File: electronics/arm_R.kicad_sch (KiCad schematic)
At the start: 26 parts, among them J10 EV3 R 4434 HOLD, J20 R SERVO G + S, U10 DRV8871DDAR, U20 SN74LVC2G17DBVR, U30 SN74AHCT1G125DBVR

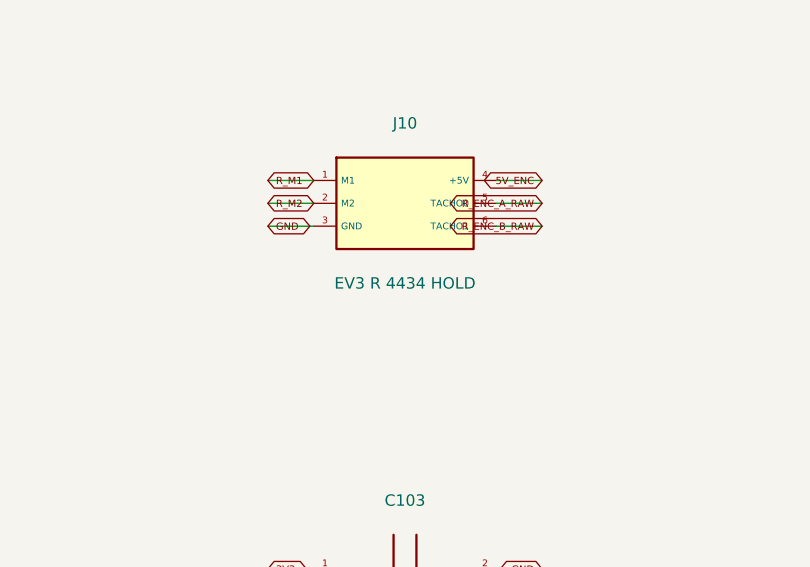
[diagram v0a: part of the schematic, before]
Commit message: Integrate onboard RP2040 and drawing-based EV3 jacks on A1 PCB
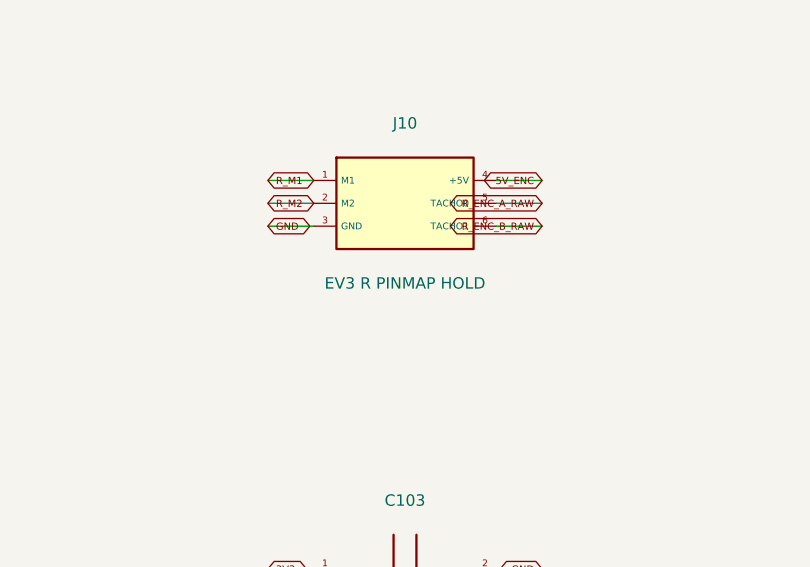
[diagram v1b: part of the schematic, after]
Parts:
- J10: value EV3 R 4434 HOLD -> EV3 R PINMAP HOLD; footprint Quadcuber:EV3_4434_PROVISIONAL -> Quadcuber:EV3_UserDrawing_PINMAP_HOLD; MPN 4434 -> UNCONFIRMED user drawing; Manufacturer Adafruit (supplier brand) -> Unconfirmed (Coorle watermark)
- TP10, TP11, TP12, TP13: now left out of the parts list
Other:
- title: Quadcuber A0 / arm_R / ENGINEERING HOLD -> Quadcuber A1 / arm_R / ENGINEERING HOLD

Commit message: Correct audited power BOM and add bounded VM discharge protection
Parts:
- C101: MPN GRM32ER71E106KA12L -> GRM32DR71E106KA12L
- F10: footprint Quadcuber:Fuse_1812_4532Metric -> Quadcuber:Fuse_Bourns_MF_MSMF_Style2_1812; MPN MF-MSMF110-2 -> MF-MSMF110/16X-2

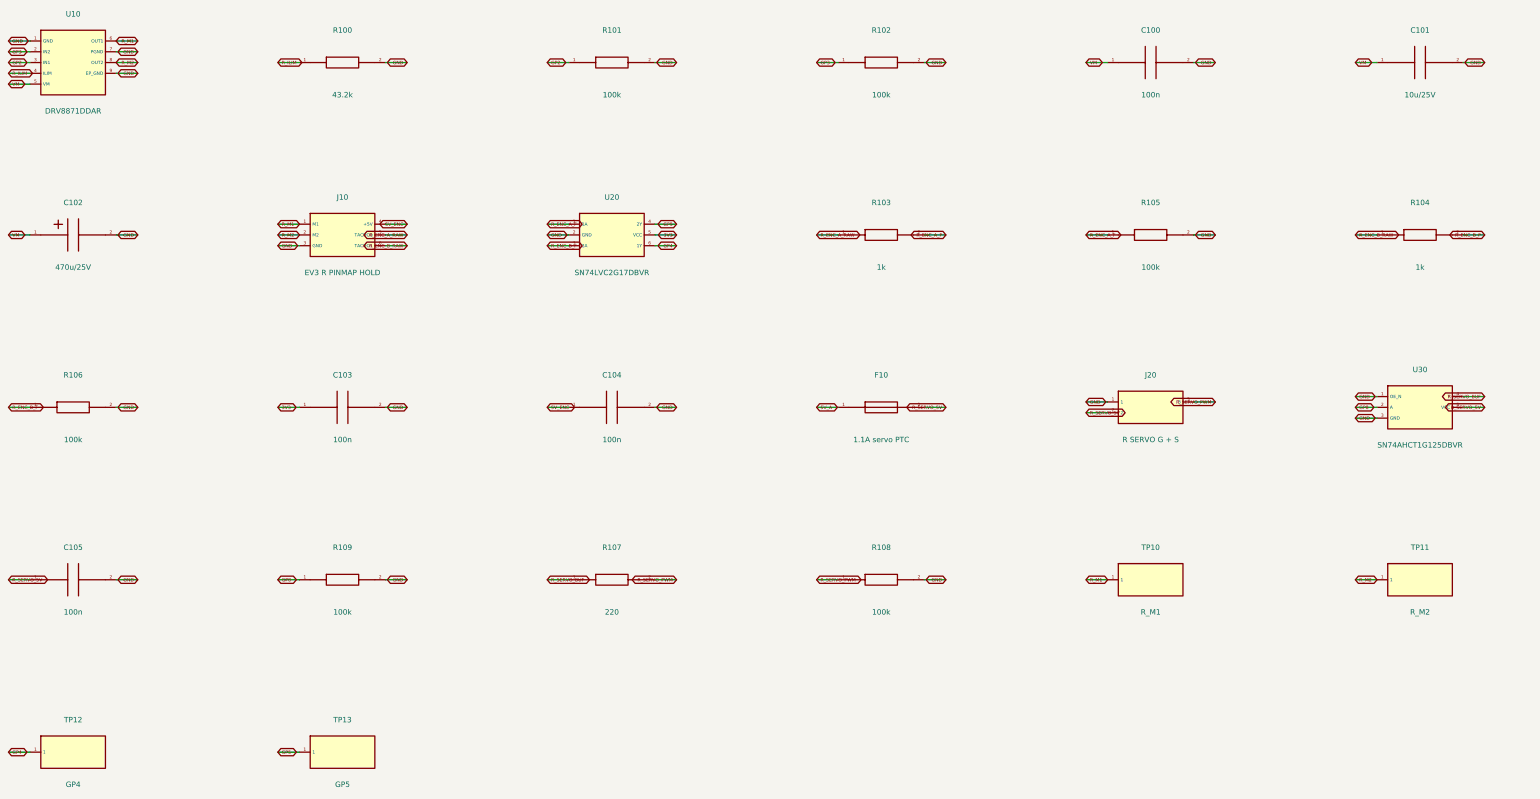
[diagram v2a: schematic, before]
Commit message: Migrate A1 to KiCad 10 and record blocked vendor-model transients
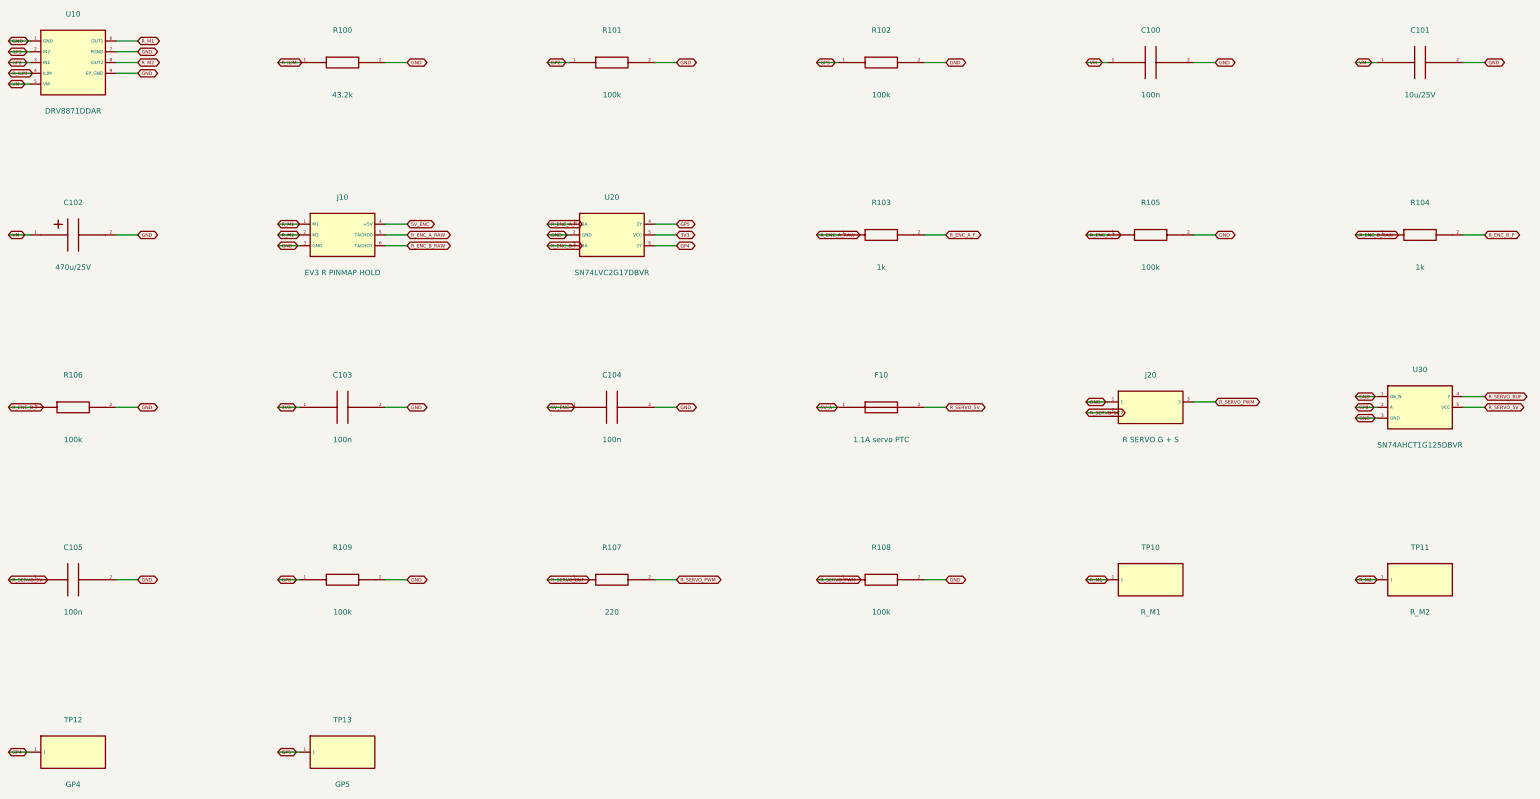
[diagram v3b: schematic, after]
